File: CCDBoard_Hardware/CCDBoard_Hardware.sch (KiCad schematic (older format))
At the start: 19 parts

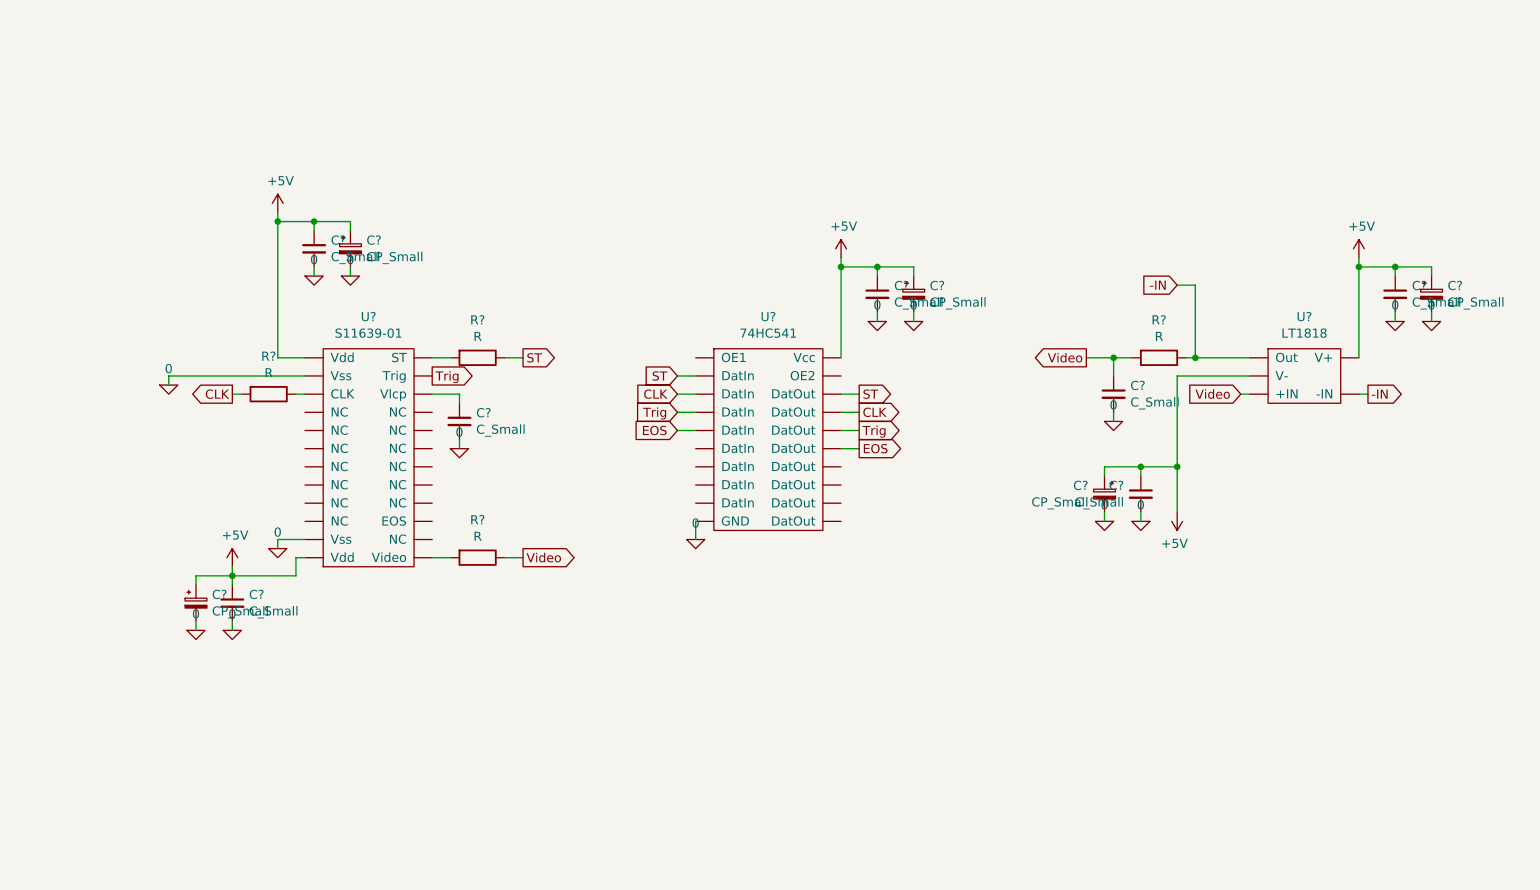
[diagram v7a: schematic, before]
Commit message: Fixed ground issues
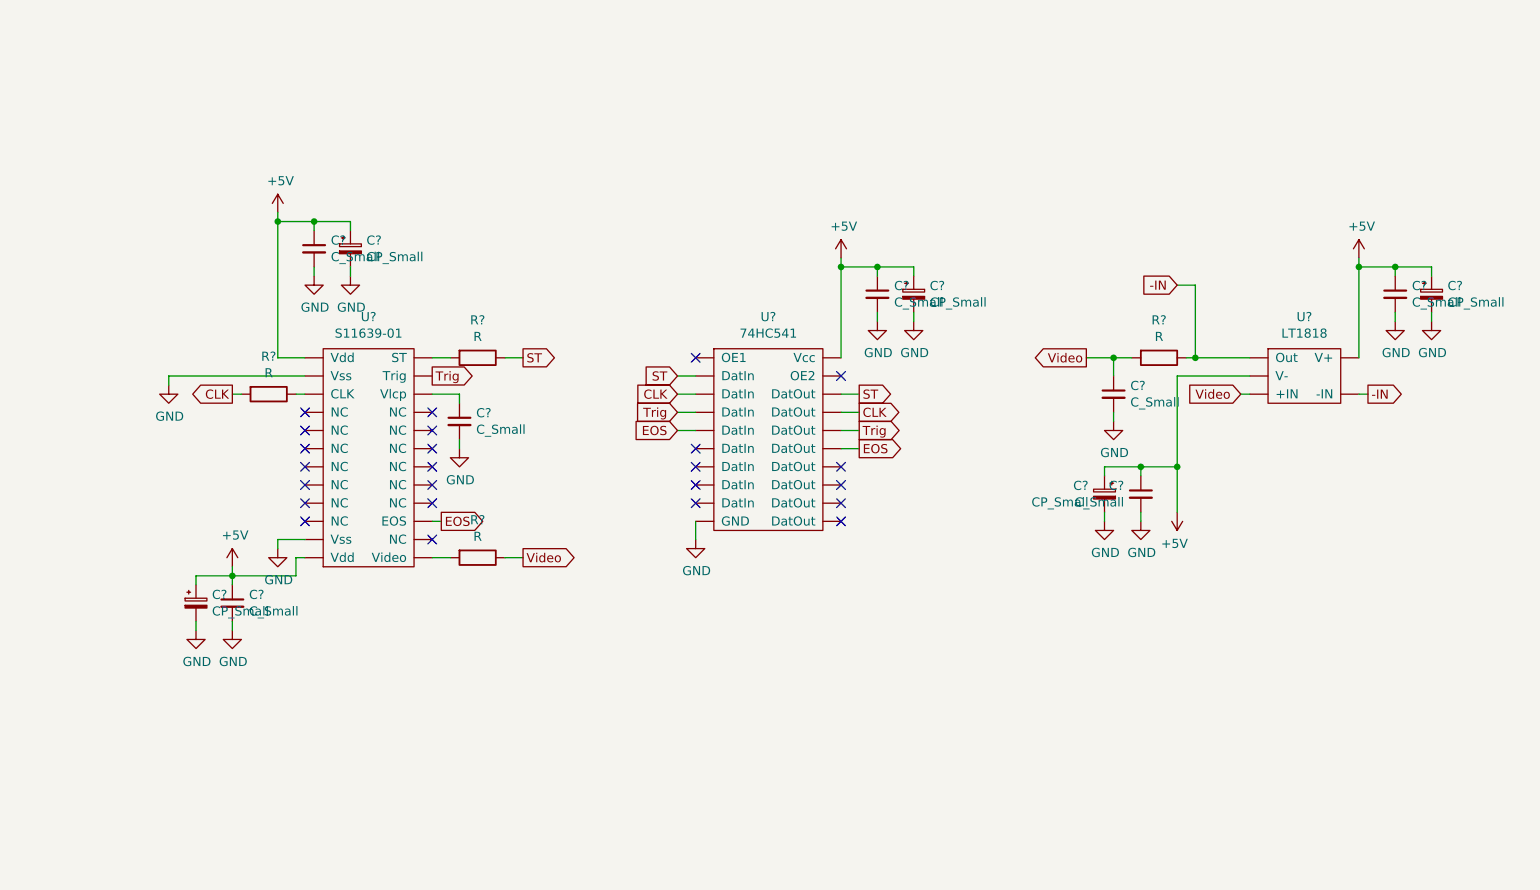
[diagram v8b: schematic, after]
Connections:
- net EOS: now also U?.~ (Vss)
- net 0 renamed GND
- no-connect marks 0 -> 24
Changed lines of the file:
@@
 Wire Wire Line
 	1850 2600 1850 2650
-$Comp
-L pspice:0 #GND?
-U 1 1 5D99AD67
-P 1850 2650
-F 0 "#GND?" H 1850 2550 50  0001 C CNN
-F 1 "0" H 1850 2739 50  0000 C CNN
-F 2 "" H 1850 2650 50  0001 C CNN
-F 3 "~" H 1850 2650 50  0001 C CNN
-	1    1850 2650
-	1    0    0    -1
-$EndComp
 Wire Wire Line
 	2550 3700 2550 3600
@@
 Wire Wire Line
 	2450 1750 2450 2500
-$Comp
-L pspice:0 #GND?
-U 1 1 5D9A4F95
-P 2650 2050
-F 0 "#GND?" H 2650 1950 50  0001 C CNN
-F 1 "0" H 2650 2139 50  0000 C CNN
-F 2 "" H 2650 2050 50  0001 C CNN
-F 3 "~" H 2650 2050 50  0001 C CNN
-	1    2650 2050
-	1    0    0    -1
-$EndComp
-$Comp
-L pspice:0 #GND?
-U 1 1 5D9A5245
-P 2850 2050
-F 0 "#GND?" H 2850 1950 50  0001 C CNN
-F 1 "0" H 2850 2139 50  0000 C CNN
-F 2 "" H 2850 2050 50  0001 C CNN
-F 3 "~" H 2850 2050 50  0001 C CNN
-	1    2850 2050
-	1    0    0    -1
-$EndComp
 $Comp
 L Device:R R?
@@
 	1    0    0    -1
 $EndComp
-$Comp
-L pspice:0 #GND?
-U 1 1 5D9AA1A5
-P 3450 3000
-F 0 "#GND?" H 3450 2900 50  0001 C CNN
-F 1 "0" H 3450 3089 50  0000 C CNN
-F 2 "" H 3450 3000 50  0001 C CNN
-F 3 "~" H 3450 3000 50  0001 C CNN
-	1    3450 3000
-	1    0    0    -1
-$EndComp
 Wire Wire Line
 	3450 2950 3450 3000
 Wire Wire Line
 	2000 3950 2000 4000
-$Comp
-L pspice:0 #GND?
-U 1 1 5D99A1EF
-P 2000 4000
-F 0 "#GND?" H 2000 3900 50  0001 C CNN
-F 1 "0" H 2000 4089 50  0000 C CNN
-F 2 "" H 2000 4000 50  0001 C CNN
-F 3 "~" H 2000 4000 50  0001 C CNN
-	1    2000 4000
-	1    0    0    -1
-$EndComp
 $Comp
 L Device:CP_Small C?
@@
 Wire Wire Line
 	2000 3700 2000 3750
-$Comp
-L pspice:0 #GND?
-U 1 1 5D997298
-P 2200 4000
-F 0 "#GND?" H 2200 3900 50  0001 C CNN
-F 1 "0" H 2200 4089 50  0000 C CNN
-F 2 "" H 2200 4000 50  0001 C CNN
-F 3 "~" H 2200 4000 50  0001 C CNN
-	1    2200 4000
-	1    0    0    -1
-$EndComp
 Wire Wire Line
 	2200 3950 2200 4000
@@
 Wire Wire Line
 	2550 3700 2200 3700
-$Comp
-L pspice:0 #GND?
-U 1 1 5D9938EB
-P 2450 3550
-F 0 "#GND?" H 2450 3450 50  0001 C CNN
-F 1 "0" H 2450 3639 50  0000 C CNN
-F 2 "" H 2450 3550 50  0001 C CNN
-F 3 "~" H 2450 3550 50  0001 C CNN
-	1    2450 3550
-	1    0    0    -1
-$EndComp
 Wire Wire Line
 	2450 3500 2450 3550
@@
 Wire Wire Line
 	5950 2250 5950 2300
-$Comp
-L pspice:0 #GND?
-U 1 1 5D99BF96
-P 5750 2300
-F 0 "#GND?" H 5750 2200 50  0001 C CNN
-F 1 "0" H 5750 2389 50  0000 C CNN
-F 2 "" H 5750 2300 50  0001 C CNN
-F 3 "~" H 5750 2300 50  0001 C CNN
-	1    5750 2300
-	1    0    0    -1
-$EndComp
-$Comp
-L pspice:0 #GND?
-U 1 1 5D99BF9C
-P 5950 2300
-F 0 "#GND?" H 5950 2200 50  0001 C CNN
-F 1 "0" H 5950 2389 50  0000 C CNN
-F 2 "" H 5950 2300 50  0001 C CNN
-F 3 "~" H 5950 2300 50  0001 C CNN
-	1    5950 2300
-	1    0    0    -1
-$EndComp
 Wire Wire Line
 	4650 2600 4750 2600
@@
 Wire Wire Line
 	4750 3400 4750 3500
-$Comp
-L pspice:0 #GND?
-U 1 1 5DA24E04
-P 4750 3500
-F 0 "#GND?" H 4750 3400 50  0001 C CNN
-F 1 "0" H 4750 3589 50  0000 C CNN
-F 2 "" H 4750 3500 50  0001 C CNN
-F 3 "~" H 4750 3500 50  0001 C CNN
-	1    4750 3500
-	1    0    0    -1
-$EndComp
 Text GLabel 3300 2600 2    50   Output ~ 0
 Trig
@@
 Wire Wire Line
 	7050 2800 7050 2850
-$Comp
-L pspice:0 #GND?
-U 1 1 5DA5C549
-P 7050 2850
-F 0 "#GND?" H 7050 2750 50  0001 C CNN
-F 1 "0" H 7050 2939 50  0000 C CNN
-F 2 "" H 7050 2850 50  0001 C CNN
-F 3 "~" H 7050 2850 50  0001 C CNN
-	1    7050 2850
-	1    0    0    -1
-$EndComp
 Wire Wire Line
 	7050 2500 7050 2600
@@
 Wire Wire Line
 	8800 2250 8800 2300
-$Comp
-L pspice:0 #GND?
-U 1 1 5DA5F332
-P 8600 2300
-F 0 "#GND?" H 8600 2200 50  0001 C CNN
-F 1 "0" H 8600 2389 50  0000 C CNN
-F 2 "" H 8600 2300 50  0001 C CNN
-F 3 "~" H 8600 2300 50  0001 C CNN
-	1    8600 2300
-	1    0    0    -1
-$EndComp
-$Comp
-L pspice:0 #GND?
-U 1 1 5DA5F338
-P 8800 2300
-F 0 "#GND?" H 8800 2200 50  0001 C CNN
-F 1 "0" H 8800 2389 50  0000 C CNN
-F 2 "" H 8800 2300 50  0001 C CNN
-F 3 "~" H 8800 2300 50  0001 C CNN
-	1    8800 2300
-	1    0    0    -1
-$EndComp
 Wire Wire Line
 	8400 2000 8400 2500
@@
 	7000 3350 7000 3400
 $Comp
-L pspice:0 #GND?
-U 1 1 5DA75B6F
-P 7200 3400
-F 0 "#GND?" H 7200 3300 50  0001 C CNN
-F 1 "0" H 7200 3489 50  0000 C CNN
-F 2 "" H 7200 3400 50  0001 C CNN
-F 3 "~" H 7200 3400 50  0001 C CNN
-	1    7200 3400
-	-1   0    0    -1
-$EndComp
-$Comp
-L pspice:0 #GND?
-U 1 1 5DA75B75
-P 7000 3400
-F 0 "#GND?" H 7000 3300 50  0001 C CNN
-F 1 "0" H 7000 3489 50  0000 C CNN
-F 2 "" H 7000 3400 50  0001 C CNN
-F 3 "~" H 7000 3400 50  0001 C CNN
-	1    7000 3400
-	-1   0    0    -1
-$EndComp
-$Comp
 L power:+5V #PWR?
 U 1 1 5DA7E890
@@
 Wire Wire Line
 	7400 2600 7400 3100
+Wire Wire Line
+	3300 3400 3350 3400
+Text GLabel 3350 3400 2    50   Output ~ 0
+EOS
+NoConn ~ 3300 2800
+NoConn ~ 3300 2900
+NoConn ~ 3300 3000
+NoConn ~ 3300 3100
+NoConn ~ 3300 3200
+NoConn ~ 3300 3300
+NoConn ~ 2600 2800
+NoConn ~ 2600 2900
+NoConn ~ 2600 3000
+NoConn ~ 2600 3100
+NoConn ~ 2600 3200
+NoConn ~ 2600 3300
+NoConn ~ 2600 3400
+NoConn ~ 3300 3500
+NoConn ~ 4750 2500
+NoConn ~ 4750 3000
+NoConn ~ 4750 3100
+NoConn ~ 4750 3200
+NoConn ~ 4750 3300
+NoConn ~ 5550 3400
+NoConn ~ 5550 3300
+NoConn ~ 5550 3200
+NoConn ~ 5550 3100
+NoConn ~ 5550 2600
+$Comp
+L power:GND #PWR?
+U 1 1 5DB1E40B
+P 2650 2050
+F 0 "#PWR?" H 2650 1800 50  0001 C CNN
+F 1 "GND" H 2655 1877 50  0000 C CNN
+F 2 "" H 2650 2050 50  0001 C CNN
+F 3 "" H 2650 2050 50  0001 C CNN
+	1    2650 2050
+	1    0    0    -1
+$EndComp
+$Comp
+L power:GND #PWR?
+U 1 1 5DB228AC
+P 2850 2050
+F 0 "#PWR?" H 2850 1800 50  0001 C CNN
+F 1 "GND" H 2855 1877 50  0000 C CNN
+F 2 "" H 2850 2050 50  0001 C CNN
+F 3 "" H 2850 2050 50  0001 C CNN
+	1    2850 2050
+	1    0    0    -1
+$EndComp
+$Comp
+L power:GND #PWR?
+U 1 1 5DB23EEC
+P 1850 2650
+F 0 "#PWR?" H 1850 2400 50  0001 C CNN
+F 1 "GND" H 1855 2477 50  0000 C CNN
+F 2 "" H 1850 2650 50  0001 C CNN
+F 3 "" H 1850 2650 50  0001 C CNN
+	1    1850 2650
+	1    0    0    -1
+$EndComp
+$Comp
+L power:GND #PWR?
+U 1 1 5DB2546C
+P 2000 4000
+F 0 "#PWR?" H 2000 3750 50  0001 C CNN
+F 1 "GND" H 2005 3827 50  0000 C CNN
+F 2 "" H 2000 4000 50  0001 C CNN
+F 3 "" H 2000 4000 50  0001 C CNN
+	1    2000 4000
+	1    0    0    -1
+$EndComp
+$Comp
+L power:GND #PWR?
+U 1 1 5DB26991
+P 2200 4000
+F 0 "#PWR?" H 2200 3750 50  0001 C CNN
+F 1 "GND" H 2205 3827 50  0000 C CNN
+F 2 "" H 2200 4000 50  0001 C CNN
+F 3 "" H 2200 4000 50  0001 C CNN
+	1    2200 4000
+	1    0    0    -1
+$EndComp
+$Comp
+L power:GND #PWR?
+U 1 1 5DB28021
+P 3450 3000
+F 0 "#PWR?" H 3450 2750 50  0001 C CNN
+F 1 "GND" H 3455 2827 50  0000 C CNN
+F 2 "" H 3450 3000 50  0001 C CNN
+F 3 "" H 3450 3000 50  0001 C CNN
+	1    3450 3000
+	1    0    0    -1
+$EndComp
+$Comp
+L power:GND #PWR?
+U 1 1 5DB2976E
+P 2450 3550
+F 0 "#PWR?" H 2450 3300 50  0001 C CNN
+F 1 "GND" H 2455 3377 50  0000 C CNN
+F 2 "" H 2450 3550 50  0001 C CNN
+F 3 "" H 2450 3550 50  0001 C CNN
+	1    2450 3550
+	1    0    0    -1
+$EndComp
+$Comp
+L power:GND #PWR?
+U 1 1 5DB2AD90
+P 4750 3500
+F 0 "#PWR?" H 4750 3250 50  0001 C CNN
+F 1 "GND" H 4755 3327 50  0000 C CNN
+F 2 "" H 4750 3500 50  0001 C CNN
+F 3 "" H 4750 3500 50  0001 C CNN
+	1    4750 3500
+	1    0    0    -1
+$EndComp
+$Comp
+L power:GND #PWR?
+U 1 1 5DB2C39A
+P 5750 2300
+F 0 "#PWR?" H 5750 2050 50  0001 C CNN
+F 1 "GND" H 5755 2127 50  0000 C CNN
+F 2 "" H 5750 2300 50  0001 C CNN
+F 3 "" H 5750 2300 50  0001 C CNN
+	1    5750 2300
+	1    0    0    -1
+$EndComp
+$Comp
+L power:GND #PWR?
+U 1 1 5DB2D8BD
+P 5950 2300
+F 0 "#PWR?" H 5950 2050 50  0001 C CNN
+F 1 "GND" H 5955 2127 50  0000 C CNN
+F 2 "" H 5950 2300 50  0001 C CNN
+F 3 "" H 5950 2300 50  0001 C CNN
+	1    5950 2300
+	1    0    0    -1
+$EndComp
+$Comp
+L power:GND #PWR?
+U 1 1 5DB2EFC2
+P 7050 2850
+F 0 "#PWR?" H 7050 2600 50  0001 C CNN
+F 1 "GND" H 7055 2677 50  0000 C CNN
+F 2 "" H 7050 2850 50  0001 C CNN
+F 3 "" H 7050 2850 50  0001 C CNN
+	1    7050 2850
+	1    0    0    -1
+$EndComp
+$Comp
+L power:GND #PWR?
+U 1 1 5DB3063E
+P 7000 3400
+F 0 "#PWR?" H 7000 3150 50  0001 C CNN
+F 1 "GND" H 7005 3227 50  0000 C CNN
+F 2 "" H 7000 3400 50  0001 C CNN
+F 3 "" H 7000 3400 50  0001 C CNN
+	1    7000 3400
+	1    0    0    -1
+$EndComp
+$Comp
+L power:GND #PWR?
+U 1 1 5DB31B79
+P 7200 3400
+F 0 "#PWR?" H 7200 3150 50  0001 C CNN
+F 1 "GND" H 7205 3227 50  0000 C CNN
+F 2 "" H 7200 3400 50  0001 C CNN
+F 3 "" H 7200 3400 50  0001 C CNN
+	1    7200 3400
+	1    0    0    -1
+$EndComp
+$Comp
+L power:GND #PWR?
+U 1 1 5DB3312F
+P 8600 2300
+F 0 "#PWR?" H 8600 2050 50  0001 C CNN
+F 1 "GND" H 8605 2127 50  0000 C CNN
+F 2 "" H 8600 2300 50  0001 C CNN
+F 3 "" H 8600 2300 50  0001 C CNN
+	1    8600 2300
+	1    0    0    -1
+$EndComp
+$Comp
+L power:GND #PWR?
+U 1 1 5DB34764
+P 8800 2300
+F 0 "#PWR?" H 8800 2050 50  0001 C CNN
+F 1 "GND" H 8805 2127 50  0000 C CNN
+F 2 "" H 8800 2300 50  0001 C CNN
+F 3 "" H 8800 2300 50  0001 C CNN
+	1    8800 2300
+	1    0    0    -1
+$EndComp
 $EndSCHEMATC
